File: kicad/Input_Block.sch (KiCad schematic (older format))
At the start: 73 parts, among them J201 ACJS-MHDRM, J202 ACJS-MHDRM, U201 NJM4558M, U202 NJM4558M, U203 ADG621BRMZ, U204 NJM4558M, U205 NJM4558M

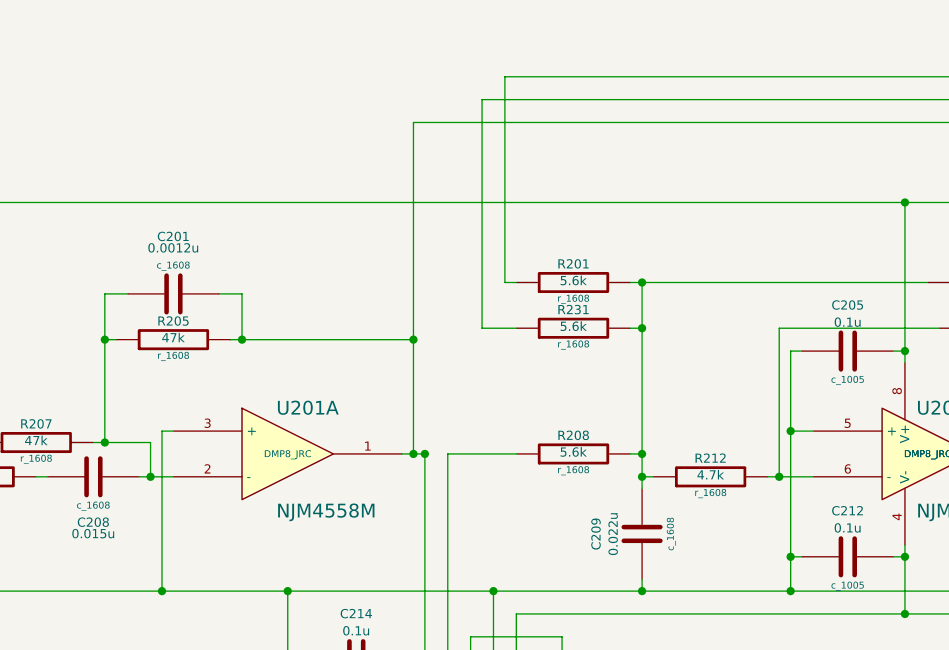
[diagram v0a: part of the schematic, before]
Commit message: Add: compander sch&pcb mod: constants
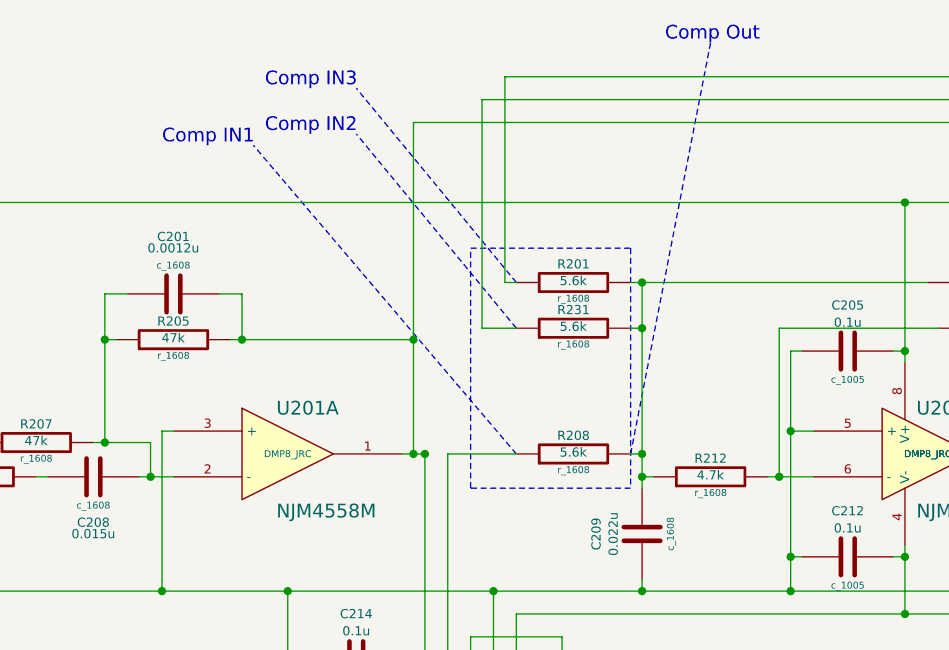
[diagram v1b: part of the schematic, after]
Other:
- note added: "Comp IN1"
- note added: "Comp IN2"
- note added: "Comp IN3"
- note added: "Comp Out"
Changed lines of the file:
@@
 LIBS:jrc
 LIBS:rohm
+LIBS:temp
+LIBS:alps
+LIBS:on_semiconductor
 LIBS:AnalogDelay-cache
 EELAYER 27 0
@@
 Sheet 2 6
 Title ""
-Date "15 dec 2013"
+Date "30 apr 2014"
 Rev ""
 Comp ""
@@
 Wire Wire Line
 	3250 7150 3500 7150
+Wire Notes Line
+	5900 2200 6600 2200
+Wire Notes Line
+	6600 2200 6600 3250
+Wire Notes Line
+	6600 3250 5900 3250
+Wire Notes Line
+	5900 3250 5900 2200
+Wire Notes Line
+	6100 2350 5400 1500
+Wire Notes Line
+	6100 2550 5400 1700
+Wire Notes Line
+	6100 3100 4950 1750
+Text Notes 4550 1750 0    60   ~ 0
+Comp IN1
+Text Notes 5000 1700 0    60   ~ 0
+Comp IN2
+Text Notes 5000 1500 0    60   ~ 0
+Comp IN3
+Wire Notes Line
+	6600 3100 6950 1300
+Text Notes 6750 1300 0    60   ~ 0
+Comp Out
 $EndSCHEMATC

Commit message: mod: Schematics
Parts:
- removed R201, R208, R216, R223, R231, R232: 5.6k, r_1608, symbol R_1608
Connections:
- net compressor/OUT1: now reaches C209.2, R202.1, R212.1
- net compressor/IN1_1: now reaches U203.2 (D1)
- net compressor/IN2_1: now reaches U203.7 (S2)
- net compressor/OUT2: now reaches C227.2, R217.1, R227.1
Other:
- note removed: "Comp IN1"
- note removed: "Comp IN2"
- note removed: "Comp IN3"
- note removed: "Comp Out"
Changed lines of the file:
@@
 LIBS:jrc
 LIBS:rohm
-LIBS:temp
 LIBS:alps
 LIBS:on_semiconductor
@@
 $Descr A3 16535 11693
 encoding utf-8
-Sheet 2 6
+Sheet 2 8
 Title ""
-Date "30 apr 2014"
+Date "8 jun 2014"
 Rev ""
 Comp ""
@@
 F 3 "~" H 4600 2600 30  0000 C CNN
 	1    4600 2600
-	0    -1   -1   0
-$EndComp
-$Comp
-L R_1608 R208
-U 1 1 5271FE2E
-P 6350 3100
-F 0 "R208" V 6430 3100 40  0000 C CNN
-F 1 "5.6k" V 6357 3101 40  0000 C CNN
-F 2 "r_1608" V 6280 3100 30  0000 C CNN
-F 3 "~" H 6350 3100 30  0000 C CNN
-	1    6350 3100
-	0    -1   -1   0
-$EndComp
-$Comp
-L R_1608 R201
-U 1 1 5266FA65
-P 6350 2350
-F 0 "R201" V 6430 2350 40  0000 C CNN
-F 1 "5.6k" V 6357 2351 40  0000 C CNN
-F 2 "r_1608" V 6280 2350 30  0000 C CNN
-F 3 "~" H 6350 2350 30  0000 C CNN
-	1    6350 2350
 	0    -1   -1   0
 $EndComp
@@
 $EndComp
 $Comp
-L R_1608 R223
-U 1 1 52886D81
-P 6350 7050
-F 0 "R223" V 6430 7050 40  0000 C CNN
-F 1 "5.6k" V 6357 7051 40  0000 C CNN
-F 2 "r_1608" V 6280 7050 30  0000 C CNN
-F 3 "~" H 6350 7050 30  0000 C CNN
-	1    6350 7050
-	0    -1   -1   0
-$EndComp
-$Comp
-L R_1608 R216
-U 1 1 52886D91
-P 6350 6300
-F 0 "R216" V 6430 6300 40  0000 C CNN
-F 1 "5.6k" V 6357 6301 40  0000 C CNN
-F 2 "r_1608" V 6280 6300 30  0000 C CNN
-F 3 "~" H 6350 6300 30  0000 C CNN
-	1    6350 6300
-	0    -1   -1   0
-$EndComp
-$Comp
 L C_1608 C227
 U 1 1 52886D97
@@
 Text HLabel 15000 1550 2    60   Input ~ 0
 FBIN2_1
-$Comp
-L R_1608 R231
-U 1 1 5297325F
-P 6350 2550
-F 0 "R231" V 6430 2550 40  0000 C CNN
-F 1 "5.6k" V 6357 2551 40  0000 C CNN
-F 2 "r_1608" V 6280 2550 30  0000 C CNN
-F 3 "~" H 6350 2550 30  0000 C CNN
-	1    6350 2550
-	0    -1   -1   0
-$EndComp
-$Comp
-L R_1608 R232
-U 1 1 529734DF
-P 6350 6500
-F 0 "R232" V 6430 6500 40  0000 C CNN
-F 1 "5.6k" V 6357 6501 40  0000 C CNN
-F 2 "r_1608" V 6280 6500 30  0000 C CNN
-F 3 "~" H 6350 6500 30  0000 C CNN
-	1    6350 6500
-	0    -1   -1   0
-$EndComp
 Text HLabel 15000 8100 2    60   Input ~ 0
 FBIN1_2
@@
 	7200 3200 7400 3200
 Wire Wire Line
-	6650 3100 6600 3100
-Wire Wire Line
 	6650 3200 6700 3200
 Connection ~ 5650 3100
-Wire Wire Line
-	6600 2350 7900 2350
 Connection ~ 6650 3200
 Wire Wire Line
@@
 Wire Wire Line
 	6650 2350 6650 3250
-Connection ~ 6650 2350
 Wire Wire Line
 	7400 3000 7300 3000
@@
 Connection ~ 8450 2550
 Wire Wire Line
-	6050 2350 6050 1450
-Wire Wire Line
-	6050 1450 15000 1450
+	6500 1450 6500 4450
+Wire Wire Line
+	6500 1450 15000 1450
 Wire Wire Line
 	8400 3100 8500 3100
-Connection ~ 6650 3100
 Wire Wire Line
 	6650 3700 6650 3650
@@
 	7200 7150 7400 7150
 Wire Wire Line
-	6650 7050 6600 7050
-Wire Wire Line
 	6650 7150 6700 7150
 Wire Wire Line
-	6600 6300 7900 6300
+	6650 6300 7900 6300
 Connection ~ 6650 7150
 Wire Wire Line
 	7250 6500 7950 6500
 Wire Wire Line
-	6650 6300 6650 7200
+	6650 5200 6650 7200
 Connection ~ 6650 6300
 Wire Wire Line
@@
 Connection ~ 8450 6500
 Wire Wire Line
-	6100 6300 6050 6300
-Wire Wire Line
 	8400 7050 8500 7050
-Connection ~ 6650 7050
 Wire Wire Line
 	6650 7650 6650 7600
@@
 	5800 7050 5600 7050
 Wire Wire Line
-	5800 3100 6100 3100
+	5800 3100 6200 3100
 Wire Wire Line
 	5800 5400 15000 5400
@@
 Connection ~ 14200 3800
 Wire Wire Line
-	6050 2350 6100 2350
-Wire Wire Line
 	14000 3600 15000 3600
 Wire Wire Line
@@
 Connection ~ 6000 3700
 Wire Wire Line
-	6000 7050 6100 7050
+	6000 5500 6350 5500
 Connection ~ 5900 5600
 Wire Wire Line
@@
 	5900 4100 5900 3900
 Wire Wire Line
-	5900 3900 6300 3900
-Wire Wire Line
-	6300 3900 6300 5400
-Connection ~ 6300 5400
+	5900 3900 6250 3900
+Wire Wire Line
+	6250 3900 6250 5400
+Connection ~ 6250 5400
 Wire Wire Line
 	5700 5300 5700 5950
 Wire Wire Line
-	6000 5300 6000 7050
+	6000 5300 6000 5500
 Wire Wire Line
 	5800 5400 5800 5300
 Connection ~ 5700 5950
 Wire Wire Line
-	15000 1550 5950 1550
-Wire Wire Line
-	5950 1550 5950 2550
-Wire Wire Line
-	5950 2550 6100 2550
-Wire Wire Line
-	6600 2550 6650 2550
-Connection ~ 6650 2550
-Wire Wire Line
-	6100 6500 5850 6500
-Wire Wire Line
-	5850 6500 5850 8100
-Wire Wire Line
-	5850 8100 15000 8100
-Wire Wire Line
-	6050 8000 15000 8000
-Wire Wire Line
-	6050 6300 6050 8000
-Wire Wire Line
-	6600 6500 6650 6500
-Connection ~ 6650 6500
+	15000 1550 6400 1550
+Wire Wire Line
+	6400 1550 6400 4350
+Wire Wire Line
+	6550 4700 6550 8100
+Wire Wire Line
+	6550 8100 15000 8100
+Wire Wire Line
+	6450 8000 15000 8000
+Wire Wire Line
+	6450 4800 6450 8000
 Wire Wire Line
 	2850 3200 1950 3200
@@
 Wire Wire Line
 	3250 7150 3500 7150
-Wire Notes Line
-	5900 2200 6600 2200
-Wire Notes Line
-	6600 2200 6600 3250
-Wire Notes Line
-	6600 3250 5900 3250
-Wire Notes Line
-	5900 3250 5900 2200
-Wire Notes Line
-	6100 2350 5400 1500
-Wire Notes Line
-	6100 2550 5400 1700
-Wire Notes Line
-	6100 3100 4950 1750
-Text Notes 4550 1750 0    60   ~ 0
-Comp IN1
-Text Notes 5000 1700 0    60   ~ 0
-Comp IN2
-Text Notes 5000 1500 0    60   ~ 0
-Comp IN3
-Wire Notes Line
-	6600 3100 6950 1300
-Text Notes 6750 1300 0    60   ~ 0
-Comp Out
+$Sheet
+S 7000 4000 1050 1050
+U 539408DE
+F0 "compressor" 50
+F1 "compander.sch" 50
+F2 "VOUT" O R 8050 4100 60
+F3 "OUT1" O R 8050 4250 60
+F4 "GND" U L 7000 4950 60
+F5 "IN1_3" I L 7000 4450 60
+F6 "IN1_2" I L 7000 4350 60
+F7 "IN1_1" I L 7000 4250 60
+F8 "VIN" I L 7000 4100 60
+F9 "OUT2" O R 8050 4600 60
+F10 "IN2_3" I L 7000 4800 60
+F11 "IN2_2" I L 7000 4700 60
+F12 "IN2_1" I L 7000 4600 60
+$EndSheet
+Wire Wire Line
+	6200 3100 6200 4250
+Wire Wire Line
+	6200 4250 7000 4250
+Wire Wire Line
+	6400 4350 7000 4350
+Wire Wire Line
+	6500 4450 7000 4450
+Wire Wire Line
+	6650 2350 7900 2350
+Wire Wire Line
+	6650 3100 6600 3100
+Wire Wire Line
+	6600 3100 6600 3900
+Wire Wire Line
+	6600 3900 8400 3900
+Wire Wire Line
+	8400 3900 8400 4250
+Wire Wire Line
+	8400 4250 8050 4250
+Connection ~ 6650 3100
+Wire Wire Line
+	6350 5500 6350 4600
+Wire Wire Line
+	6350 4600 7000 4600
+Wire Wire Line
+	6550 4700 7000 4700
+Wire Wire Line
+	6450 4800 7000 4800
+Wire Wire Line
+	8050 4600 8400 4600
+Wire Wire Line
+	8400 4600 8400 5200
+Wire Wire Line
+	8400 5200 6650 5200
 $EndSCHEMATC
